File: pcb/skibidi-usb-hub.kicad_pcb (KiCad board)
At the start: 4 copper layers, 50 x 65 mm, 115 parts, among them SW1 B3U-1100PM, SW2 B3U-1100PM, T1 H1102NLT_C20623173, T2 H1102NLT_C20623173, U1 CH334F_C5187527, U10 PJ-320A-4P DIP, U2 CH217K, U3 GT-USB-7010ASV, U4 GT-USB-7010ASV, U5 RTL8152B-VB-CG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

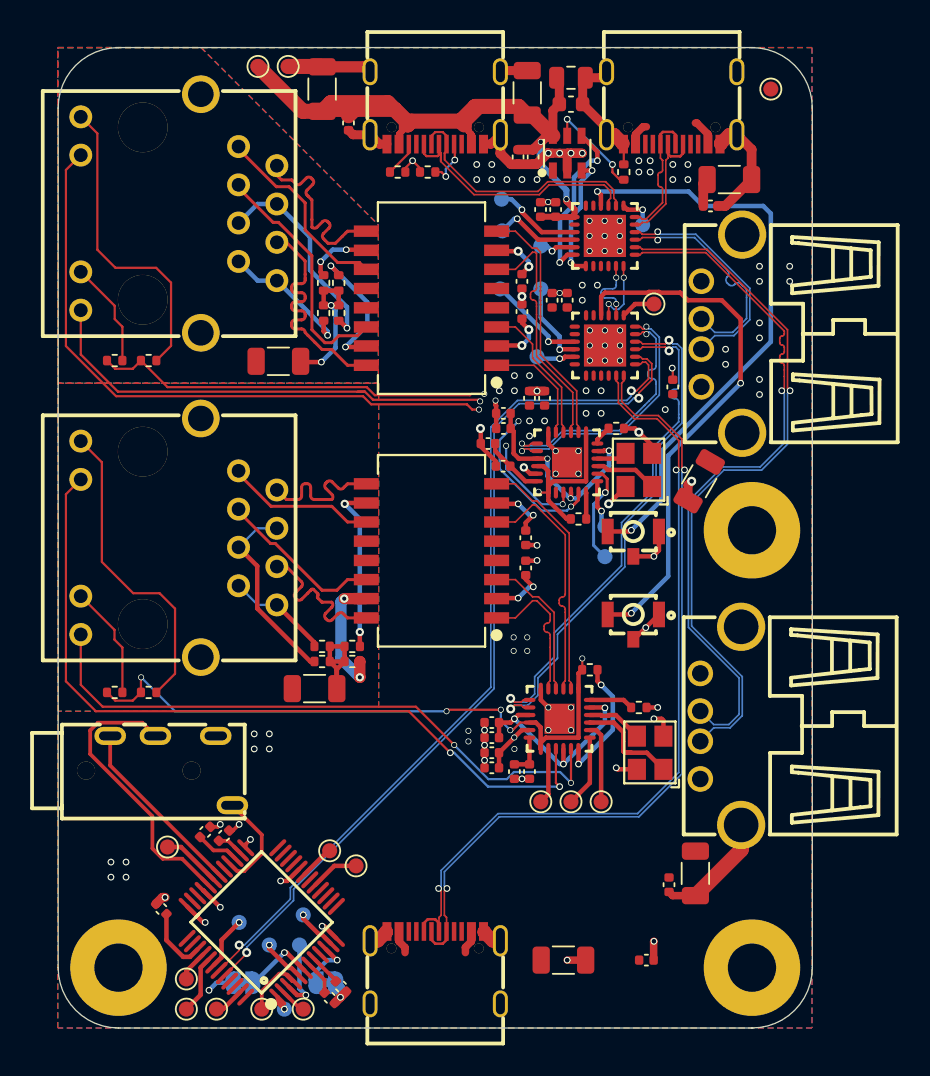
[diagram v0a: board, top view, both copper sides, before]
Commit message: add bom, update src, add readme
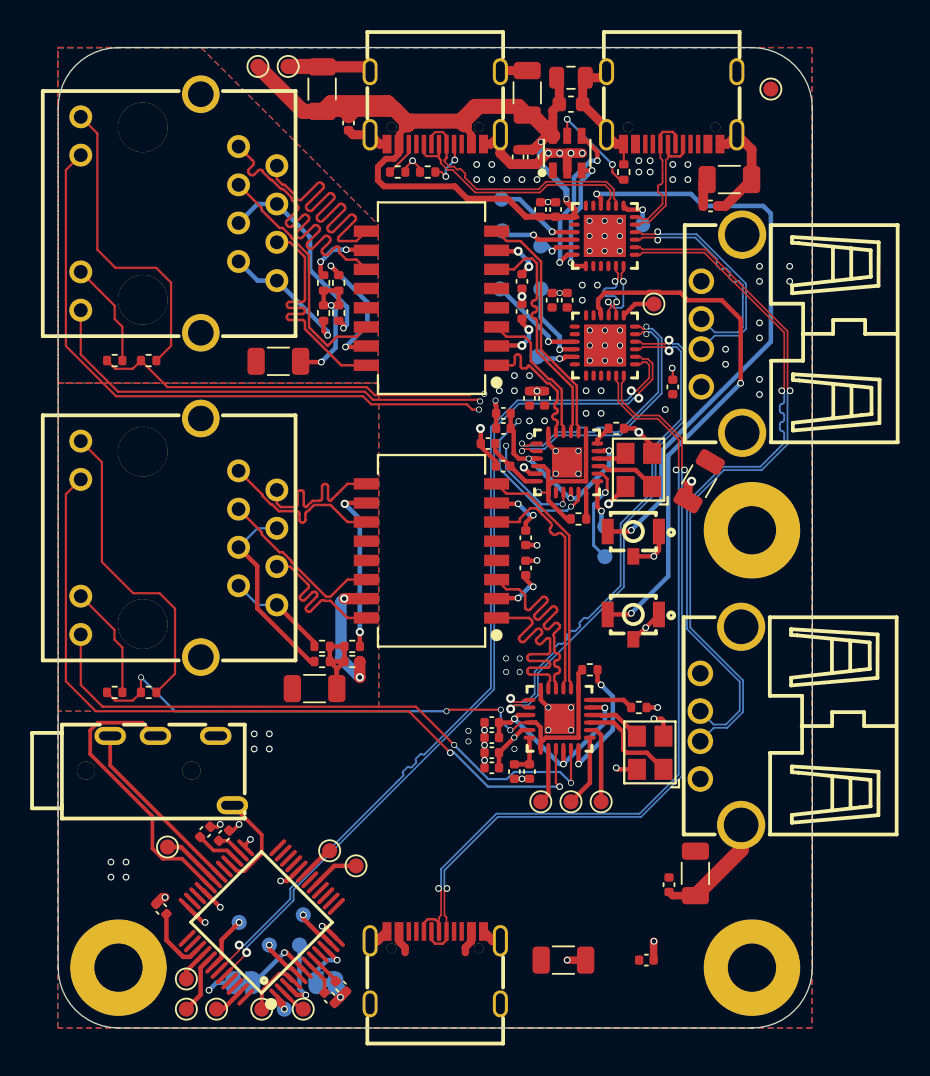
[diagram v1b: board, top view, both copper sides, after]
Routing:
- net VBUS: track 61.4 -> 76.5 mm
- net /TDI0-: track 12.9 -> 22.7 mm
- net /TDI0+: track 13.0 -> 22.7 mm
- net /MDI3+: track 9.81 -> 16.7 mm
- net /MDI3-: track 9.81 -> 16.7 mm
- net +5V: track 13.1 -> 9.68 mm
- net /MDI1-: track 7.62 -> 9.54 mm
- net /TDI2-: track 9.92 -> 11.4 mm
- net /TDI2+: track 9.99 -> 11.4 mm
- net /MDI0-: track 16.9 -> 16.1 mm
- net /MDI0+: track 16.9 -> 16.1 mm
- net +3.3V3: track 42.3 -> 41.6 mm, vias 5 -> 4
- net Net-(U1-LED1): track 5.69 -> 5.03 mm
